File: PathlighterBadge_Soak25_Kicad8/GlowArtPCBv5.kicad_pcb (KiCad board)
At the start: 2 copper layers, 93.2 x 113.9 mm, 12 parts, among them SW1 SW_SPDT

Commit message: More logos from old board
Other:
- board text added: "www.thereuglow.club"
- board text removed: "design files: Github.com/Drc3p0"

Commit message: Start building 3D pcb
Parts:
- removed the ? at (154.4, 41.5) (x6)
- removed flat side: LED, LED_THT:LED_D5.0mm_Horizontal_O1.27mm_Z3.0mm (x3)
- added ? (x5): , Graphics, F.Cu at (154.4, 41.5)
- added ?: , Graphics, B.Cu at (154.4, 41.5)
- added D1: LED, LED_THT:LED_D5.0mm_Horizontal_O1.27mm_Z3.0mm, B.Cu at (207.9, 81.5)
- added D2: LED, LED_THT:LED_D5.0mm_Horizontal_O1.27mm_Z3.0mm, B.Cu at (201.2, 129.3)
- added D3: LED, LED_THT:LED_D5.0mm_Horizontal_O1.27mm_Z3.0mm, B.Cu at (197.0, 81.8)
- added REF**: BugBackbone, adhoc:BugBackbone, B.Cu at (200.0, 61.2)
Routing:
- net Net-(D1-A): track 88.8 -> 92.8 mm
- net Net-(BT1--): track 109.0 -> 110.0 mm
- net (no net): vias 1 -> 0

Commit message: Scootch backbone?
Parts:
- moved REF** 4.50 mm to (200.0, 65.7)
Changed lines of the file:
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@@
 	(footprint "adhoc:BugBackbone"
 		(layer "B.Cu")
-		(at 200 61.2 180)
+		(at 200 65.7 180)
 		(property "Reference" "REF**"
 			(at 0 -29.45 0)

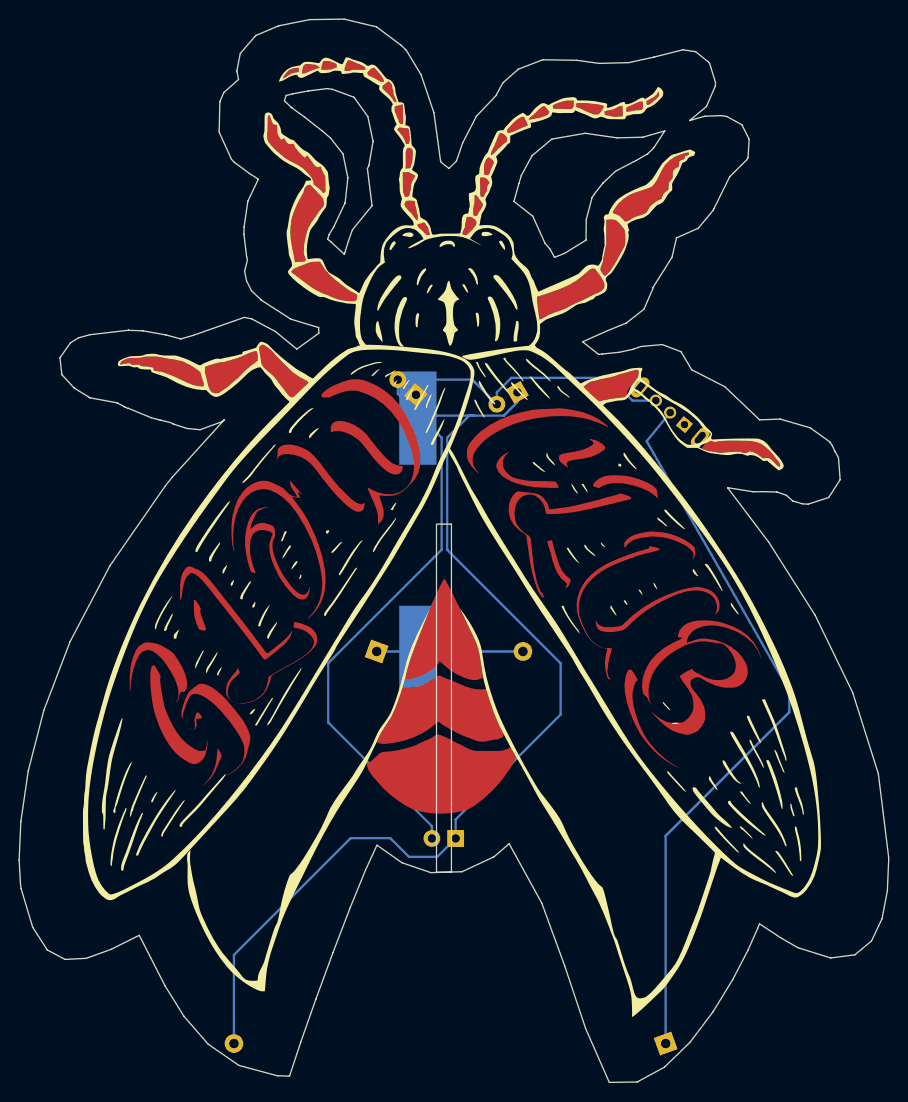
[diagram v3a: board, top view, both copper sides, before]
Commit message: Flip slots again, move logos
Slot's gotta be this way so there's room for the LED
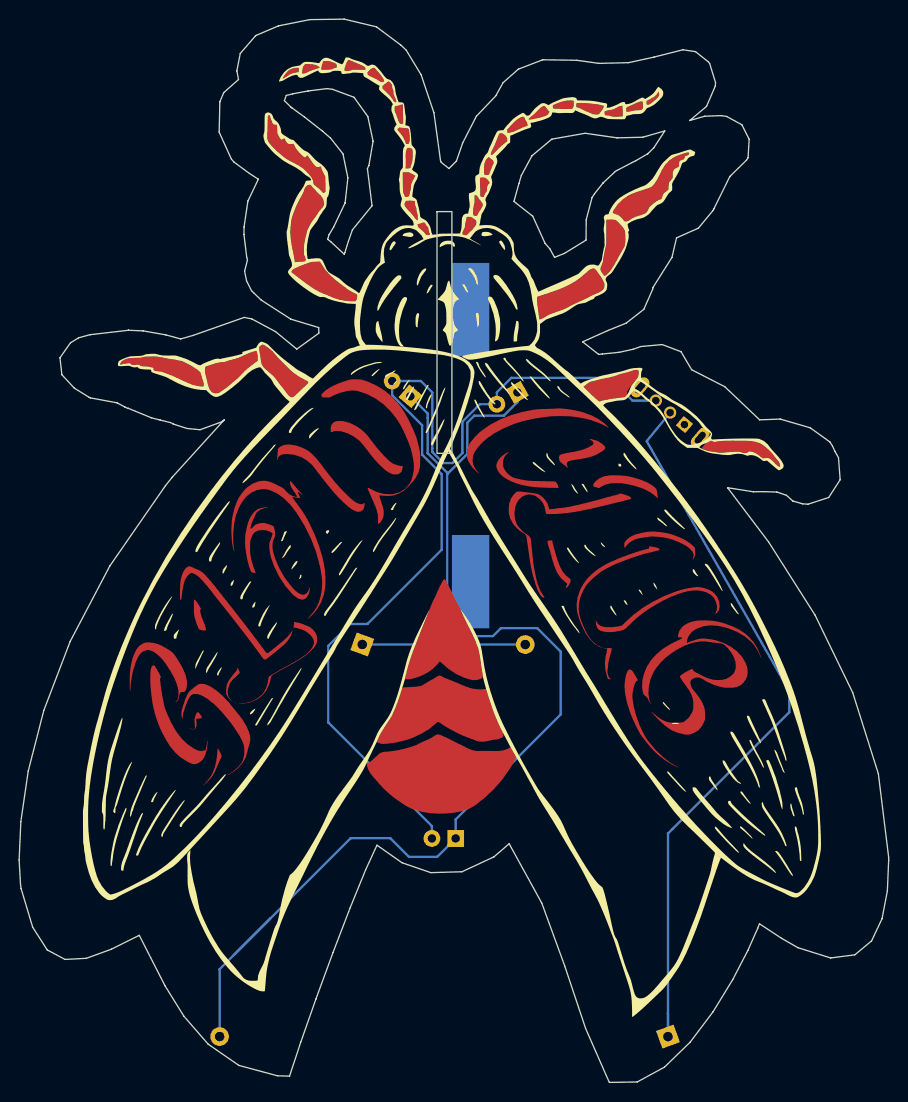
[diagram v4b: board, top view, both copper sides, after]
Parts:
- B1: renamed from REF**; footprint adhoc:BugBackbone -> footprints:BugBackbone; moved to F.Cu
- moved B1 7.58 mm to (200.1, 58.1), turned to 0 degrees
- moved BT1 1.71 mm to (191.2, 108.5)
- moved BT2 0.79 mm to (224.0, 150.5)
- moved D3 0.62 mm to (196.4, 81.9)
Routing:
- net Net-(BT1--): track 110.0 -> 124.3 mm
- net Net-(D1-A): track 92.8 -> 105.0 mm
- net Net-(BT2-+): track 78.0 -> 80.2 mm
- net Net-(BT1-+): track 15.7 -> 17.5 mm

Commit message: Tweaks from feedback
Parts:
- added ?: , clipboard:4c0663b7-a142-46c9-a736-897c05f203ad, F.Cu at (209.0, 111.0)
- moved D1 1.27 mm to (208.3, 82.7)
- moved D3 1.17 mm to (195.8, 82.9)
- moved B1 0.24 mm to (200.0, 58.4)
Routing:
- net Net-(D1-A): track 105.0 -> 115.8 mm

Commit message: Fix overlap on G/C, adjust backbone bands
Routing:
- added copper zone on F.Cu, net (none)
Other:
- board text removed: "Let your light shine so brightly that you illuminate a pathway for others to find their way out of the darkness"

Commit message: Final tweaks, hopefully!
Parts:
- removed the ? at (209.0, 111.0)
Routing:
- net Net-(D1-A): track 115.8 -> 114.0 mm
- net Net-(BT1--): track 123.9 -> 123.2 mm
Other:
- board text added: "+ -"
